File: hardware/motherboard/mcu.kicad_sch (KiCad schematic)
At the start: 22 parts, among them J10 swd-connect-3, SW1 Reset, U1 ch32v003f4u6, U11 SN74LV1T34DCK, U12 SN74LV1T34DCK, U13 SN74LV1T34DCK, U14 SN74LV1T34DCK, U8 SN74LV1T34DCK

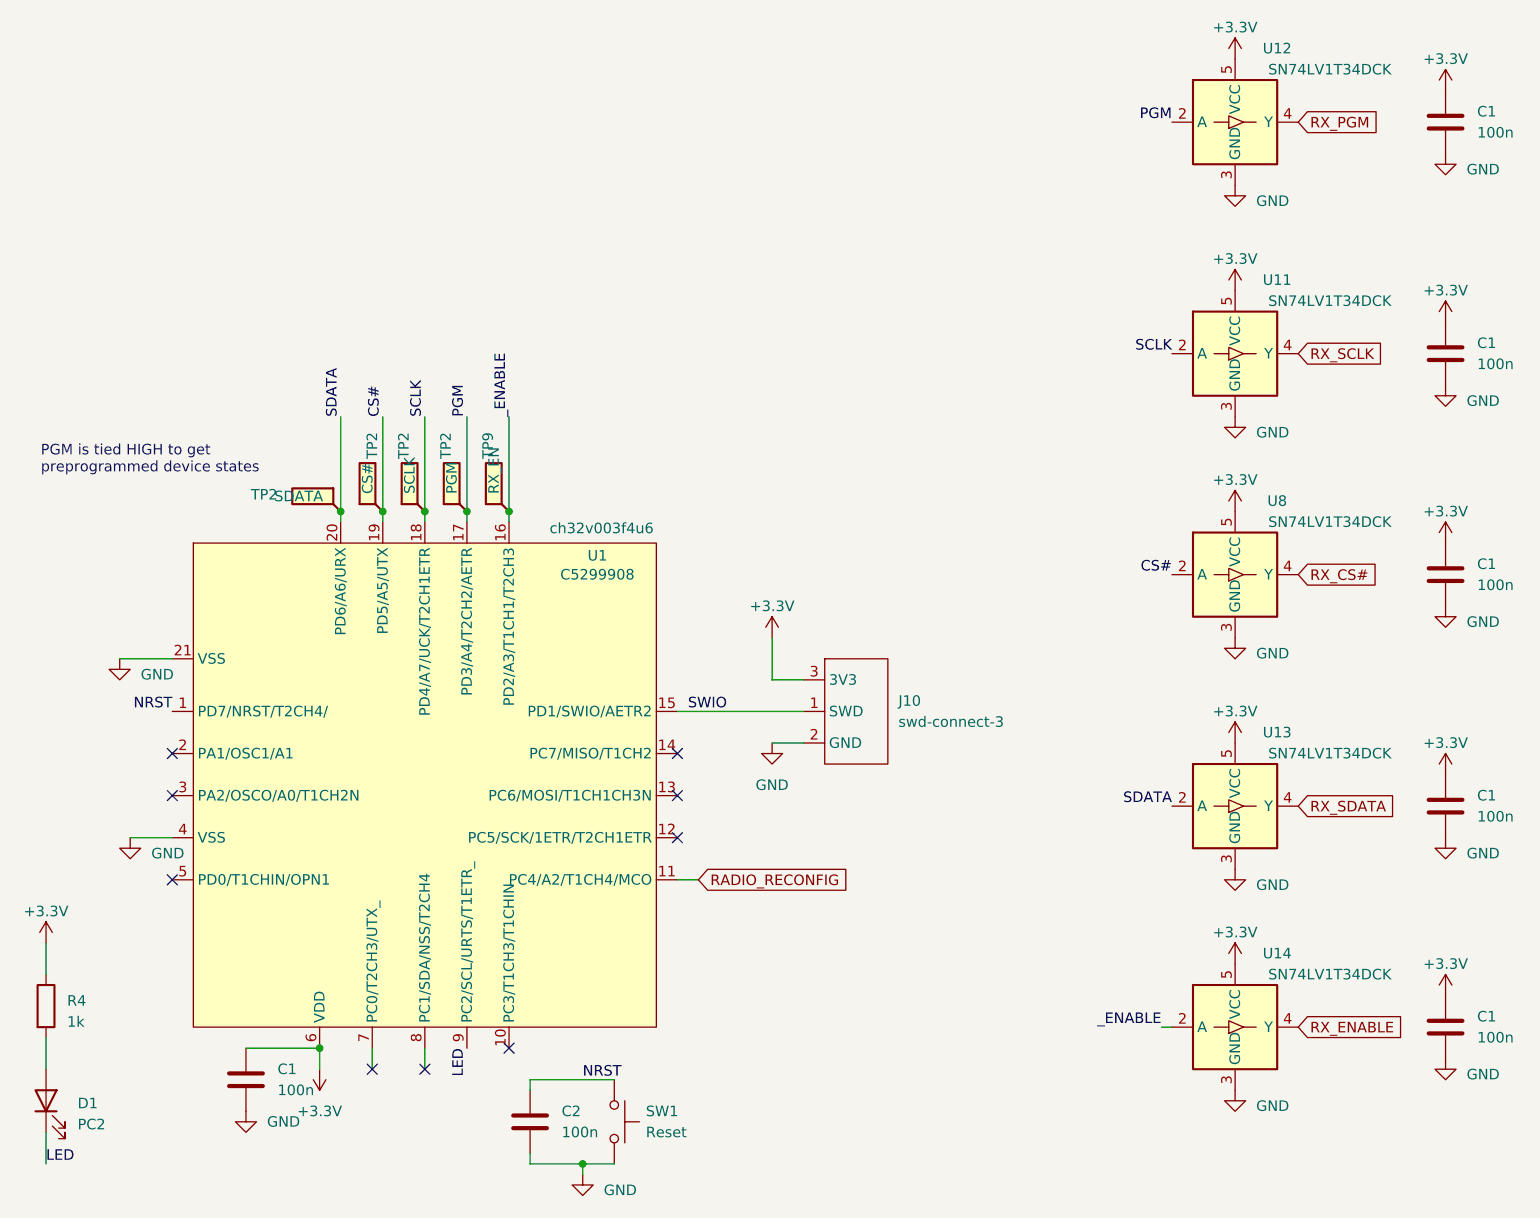
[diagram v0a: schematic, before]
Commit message: Update to KiCAD 10
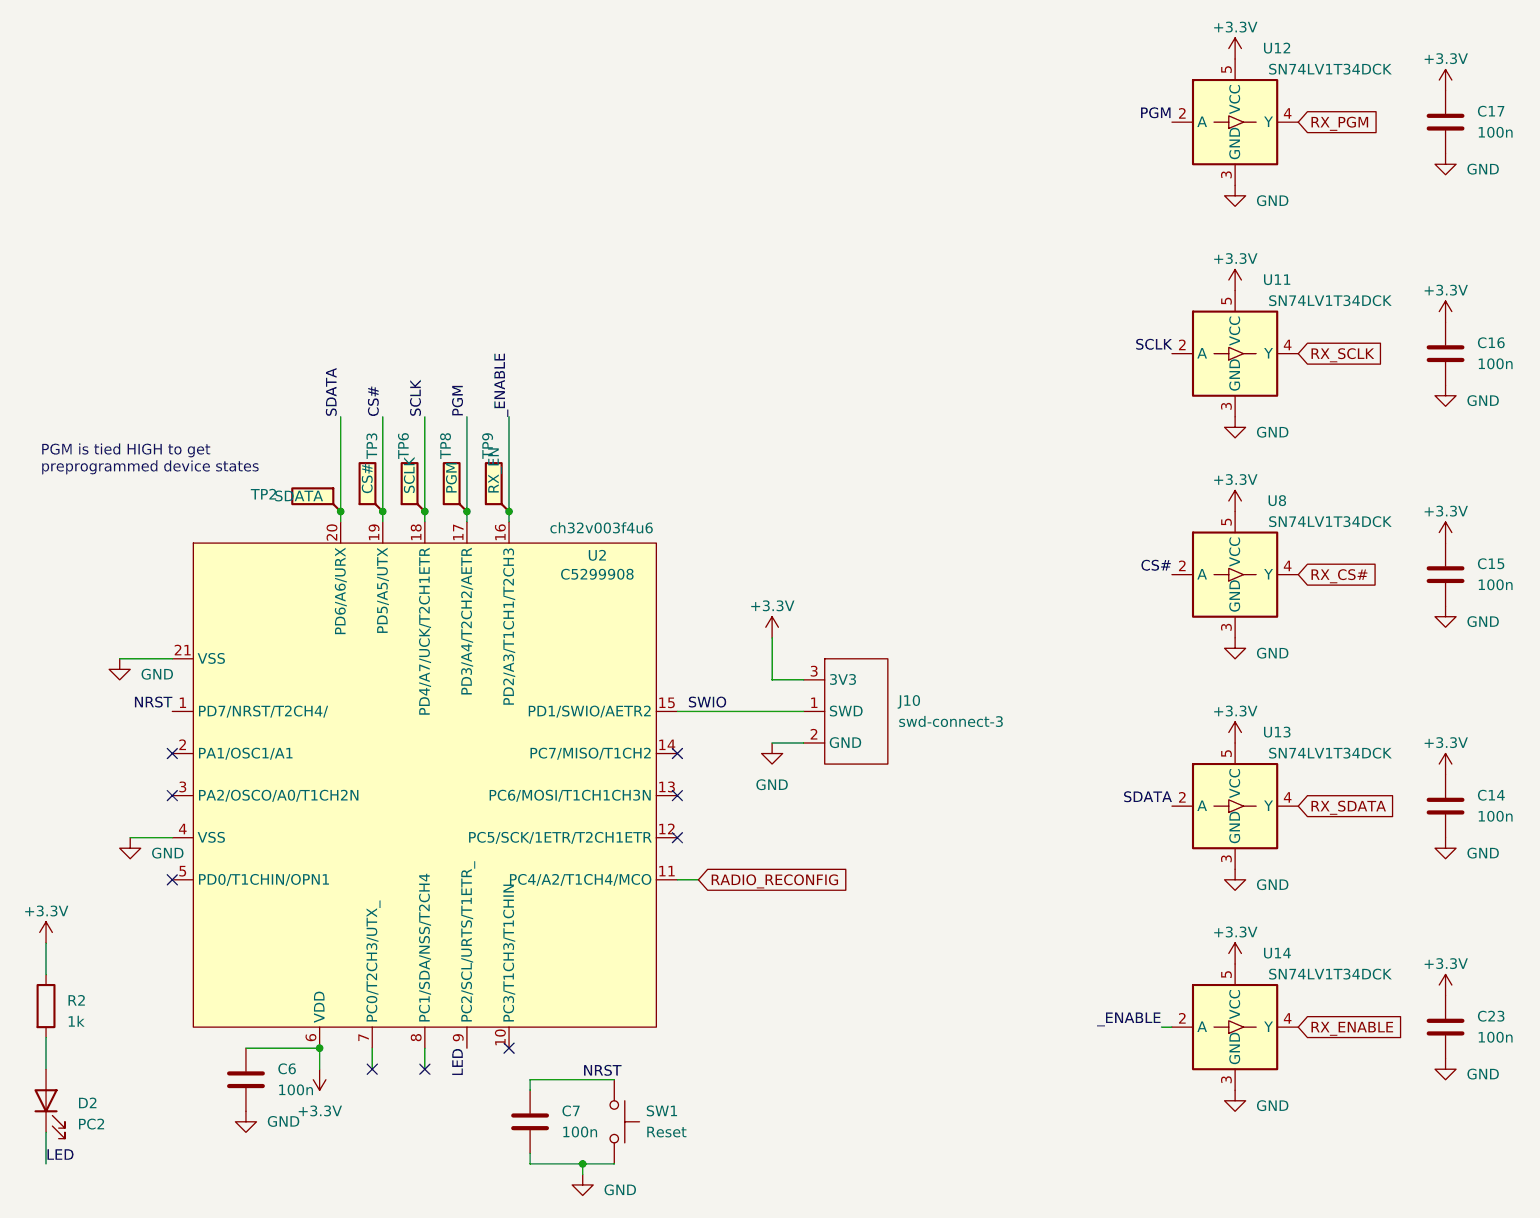
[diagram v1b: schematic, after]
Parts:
- renumbered C1 to C14, C1 to C15, C1 to C16, C1 to C17, C1 to C23, C1 to C6, C2 to C7, D1 to D2, R4 to R2, TP2 to TP3, TP2 to TP6, TP2 to TP8, U1 to U2
